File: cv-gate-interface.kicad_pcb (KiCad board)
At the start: 2 copper layers, 29.5 x 22.5 mm, 19 parts, among them J3 Conn_01x06_Pin, J4 Conn_01x06_Pin, SW1 SW_SPST, U1 TL072

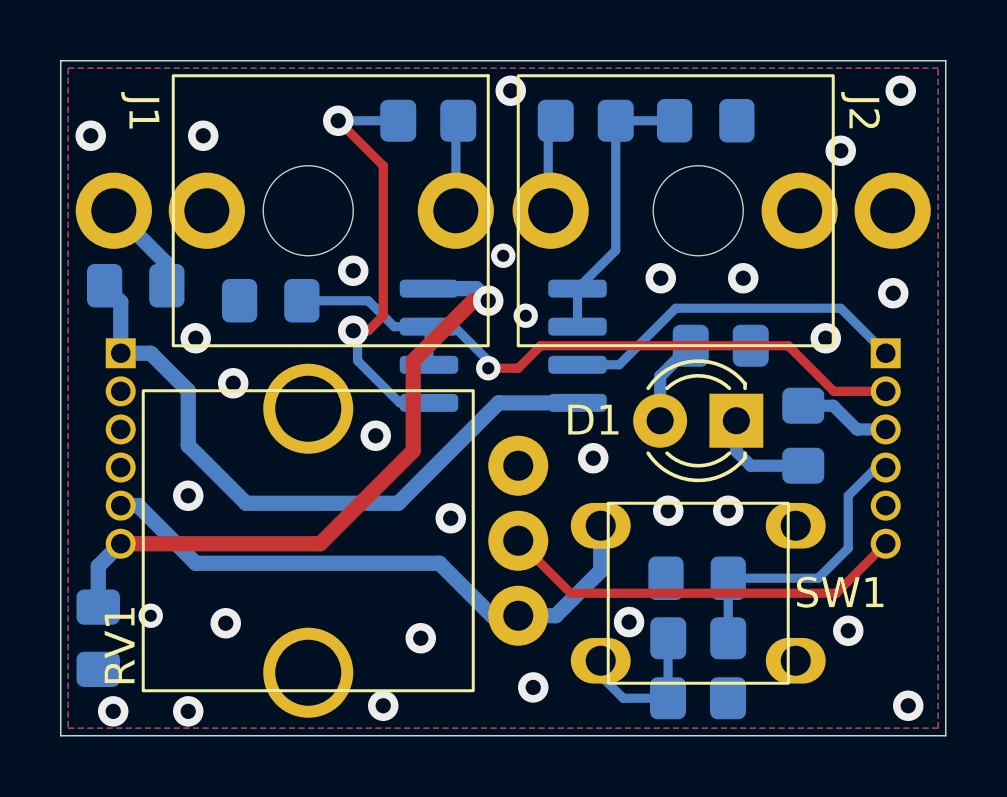
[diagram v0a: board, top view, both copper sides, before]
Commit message: Changed pot to 10K, fixed routing
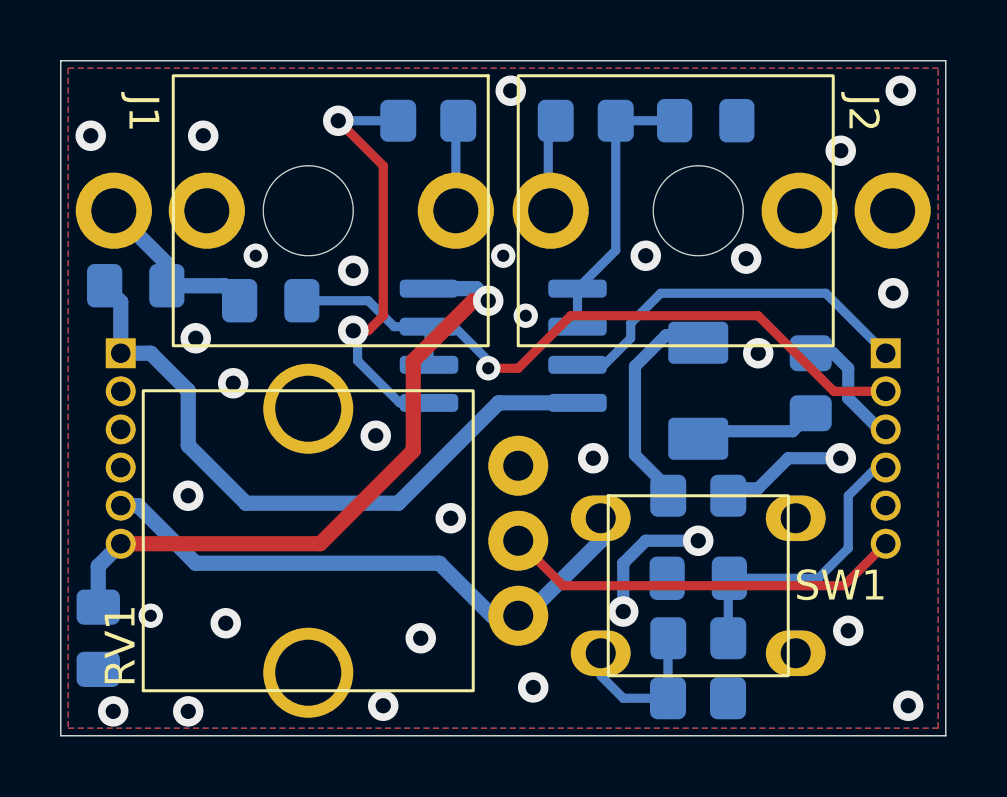
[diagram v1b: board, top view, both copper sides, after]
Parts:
- C1: value C -> 100nF
- D1: footprint LED_THT:LED_D3.0mm -> mjrskiles:XZMDKVG55W-7; moved to B.Cu
- R2: value R_US -> 1K
- R3, R4, R5: value R_US -> 220
- R6: value R_US -> 10K
- RV1: value 100K -> 10K
- moved R4 5.06 mm to (146.2, 89.5)
- moved R3 1.77 mm to (150.0, 85.8)
- moved D1 1.62 mm to (146.2, 86.0), turned to 90 degrees
- moved SW1 0.25 mm to (146.2, 92.5)
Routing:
- net GND: track 3.23 -> 14.4 mm, vias 30 -> 31
- net Net-(D1-Pad2): track 2.92 -> 7.06 mm
- net /CV_OUT_RAW: track 11.7 -> 13.0 mm
- net /LED_OUT_BUFFERED: track 3.08 -> 4.14 mm
- net /CV_IN_BUFFERED: track 22.8 -> 23.6 mm
- net Net-(D1-Pad1): track 3.45 -> 4.00 mm
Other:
- board text added: "Shapeware 1U Interface 1.0"
- board text removed: "Shapeware 1U 1.0"
